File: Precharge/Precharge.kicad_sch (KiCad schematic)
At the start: 68 parts, among them J1 Conn_01x02, J2 Conn_01x02, J3 Molex MicroFit, J4 Conn_02x03_Counter_Clockwise, K1 KT12-1A-40L-THT, Q1 CJ2310, Q2 AO3400A, Q3 AO3400A, U1 LM393, U2 4N35, U3 4N35

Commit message: Add latest circuit PDFs
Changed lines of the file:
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@@
 	)
 	(rectangle
-		(start 152.0712 239.3131)
+		(start 153.924 239.3131)
 		(end 183.8212 265.9831)
 		(stroke
@@
 		)
 	)
-	(text "Mounting Holes"
-		(exclude_from_sim no)
-		(at 168.5812 235.5031 0)
-		(effects
-			(font
-				(size 2.54 2.54)
-				(thickness 0.508)
-				(bold yes)
-			)
-		)
-	)
 	(text "3s"
 		(exclude_from_sim no)
@@
 	(text "Mounting Holes"
 		(exclude_from_sim no)
-		(at 168.5812 235.5031 0)
+		(at 168.91 235.966 0)
 		(effects
 			(font
@@
 	(wire
 		(pts
+			(xy 208.28 269.24) (xy 208.28 267.97)
+		)
+		(stroke
+			(width 0)
+			(type default)
+		)
+	)
+	(wire
+		(pts
 			(xy 218.44 119.38) (xy 229.87 119.38)
 		)
@@
 	(symbol
 		(lib_id "power:+12V")
-		(at 208.28 267.97 180)
+		(at 208.28 269.24 180)
 		(unit 1)
 		(exclude_from_sim no)
@@
 		(dnp no)
 		(property "Reference" "#PWR012"
-			(at 208.28 264.16 0)
+			(at 208.28 265.43 0)
 			(effects
 				(font
@@
 		)
 		(property "Value" "GLV+"
-			(at 208.28 271.018 90)
+			(at 208.28 272.288 90)
 			(effects
 				(font
@@
 		)
 		(property "Footprint" ""
-			(at 208.28 267.97 0)
+			(at 208.28 269.24 0)
 			(effects
 				(font
@@
 		)
 		(property "Datasheet" ""
-			(at 208.28 267.97 0)
+			(at 208.28 269.24 0)
 			(effects
 				(font
@@
 		)
 		(property "Description" ""
-			(at 208.28 267.97 0)
+			(at 208.28 269.24 0)
 			(effects
 				(font

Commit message: Add PDIST
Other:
- note added: "TS Activate Button will activate the Precharge Relay AND AIR- which connects HV- to TS-"
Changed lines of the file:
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@@
+		)
+	)
+	(text "TS Activate Button will activate the Precharge Relay AND AIR- \nwhich connects HV- to TS-"
+		(exclude_from_sim no)
+		(at 105.156 189.738 0)
+		(effects
+			(font
+				(size 1.27 1.27)
+			)
+			(justify left)
 		)
 	)

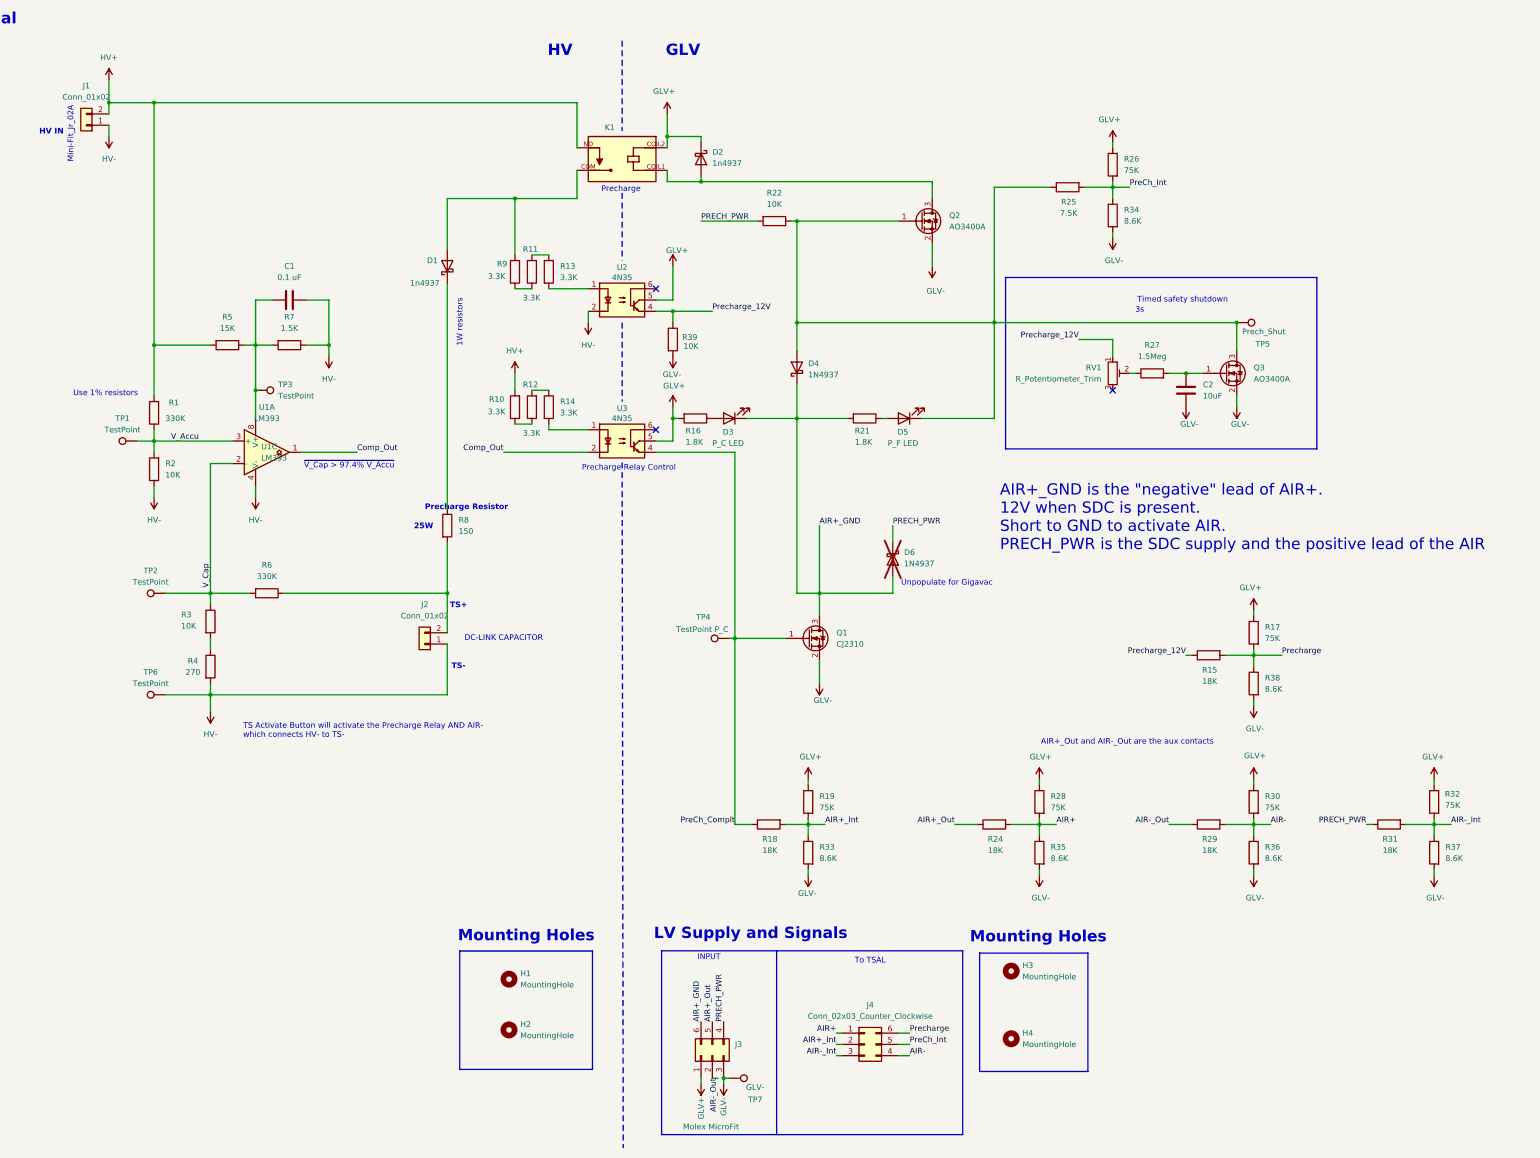
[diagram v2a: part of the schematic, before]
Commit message: added hierarchichal labels for hierarchical sheet compatibility
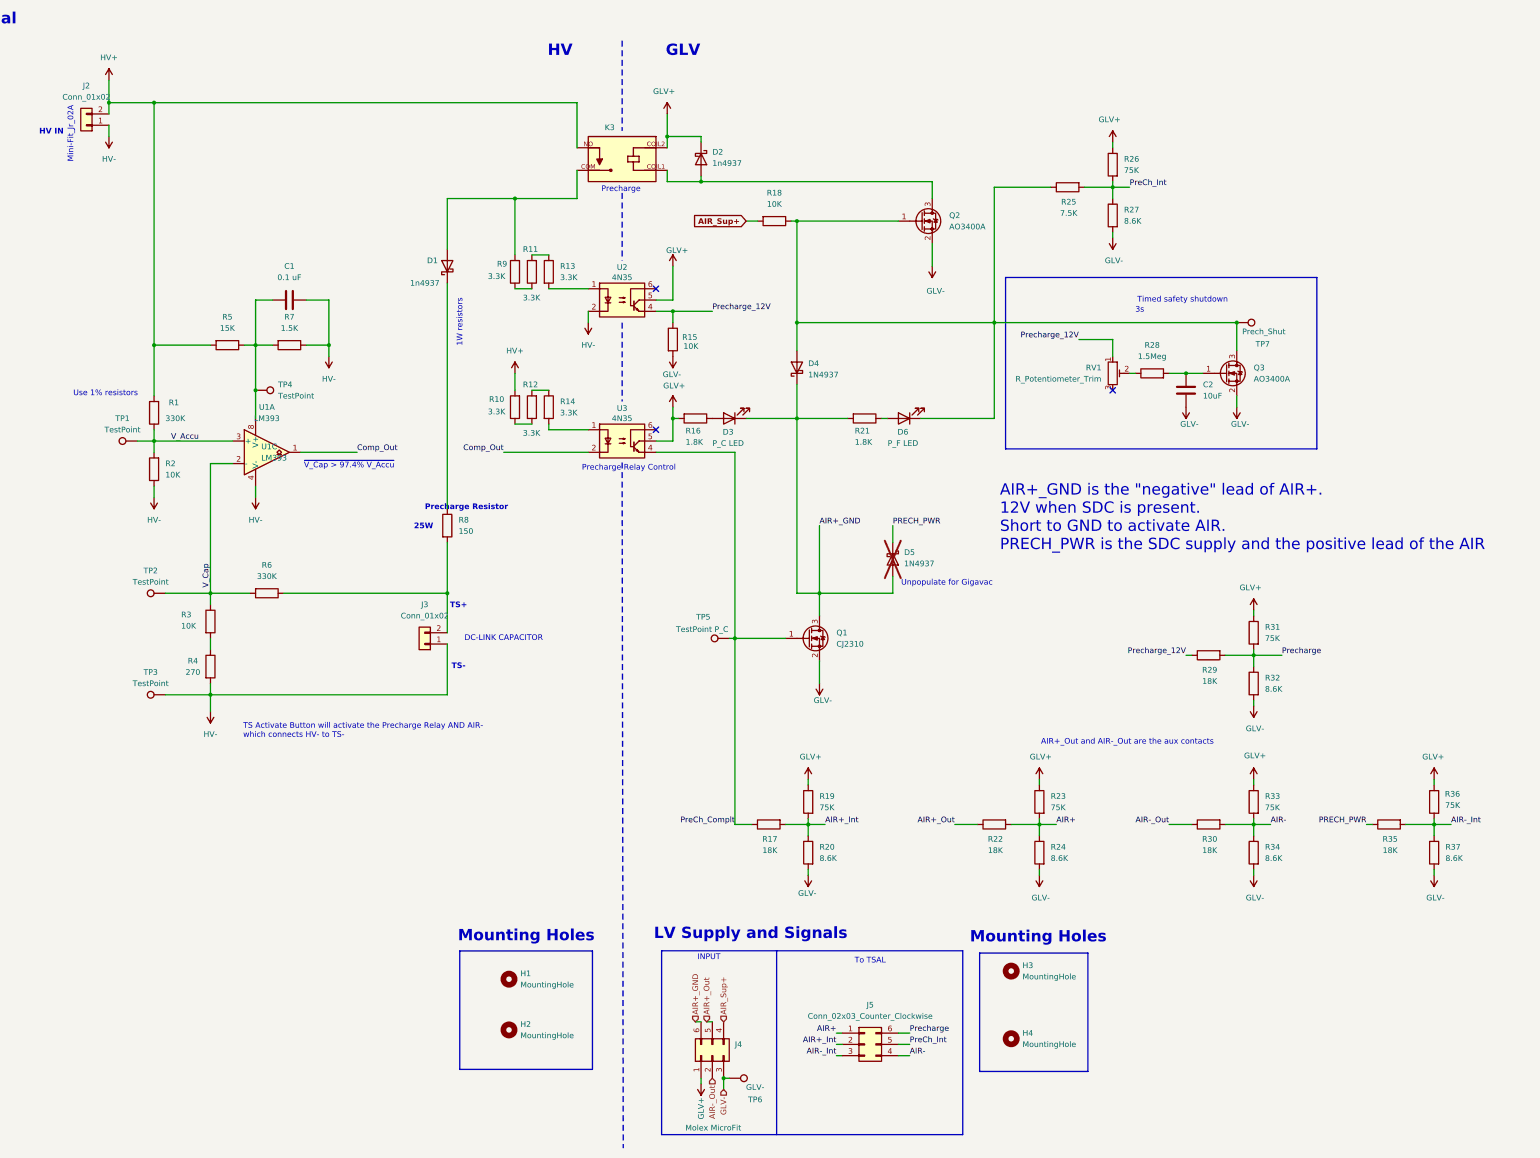
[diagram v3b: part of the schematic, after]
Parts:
- U1: footprint Package_SO:SOIC-8_3.9x4.9mm_P1.27mm -> (none)
- renumbered D6 to D5, D5 to D6, J1 to J2, J2 to J3, J3 to J4, J4 to J5, K1 to K3, R39 to R15, R18 to R17, R22 to R18, R33 to R20, R24 to R22, R28 to R23, R35 to R24, R34 to R27, R27 to R28, R15 to R29, R29 to R30, R17 to R31, R38 to R32, R30 to R33, R36 to R34, R31 to R35, R32 to R36, TP6 to TP3, TP3 to TP4, TP4 to TP5, TP7 to TP6, TP5 to TP7
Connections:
- net PRECH_PWR: no longer J4.4 (Pin_4), R18.2
- new net AIR_Sup+: J4.4 (Pin_4), R18.2

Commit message: Save corrupted files and new modifications
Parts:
- removed U1: LM393, symbol Comparator:LM393
- added U1 (x2): LM393, Package_SO:SOIC-8_3.9x4.9mm_P1.27mm, symbol Comparator:LM393
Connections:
- net PRECH_PWR is gone; now on net AIR_Sup+: D5.1 (K), R35.1
- net Comp_Out: now also U1.1, U1.1
- net V_Accu: now also U1.3 (+), U1.3 (+)
- net V_Cap: now also U1.2 (-), U1.2 (-)
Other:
- note added: "AIR_Sup+ is +12V when driver activates precharge"
